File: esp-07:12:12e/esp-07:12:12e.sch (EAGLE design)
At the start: 5 parts, among them J1 ESP-STACK-HEADER

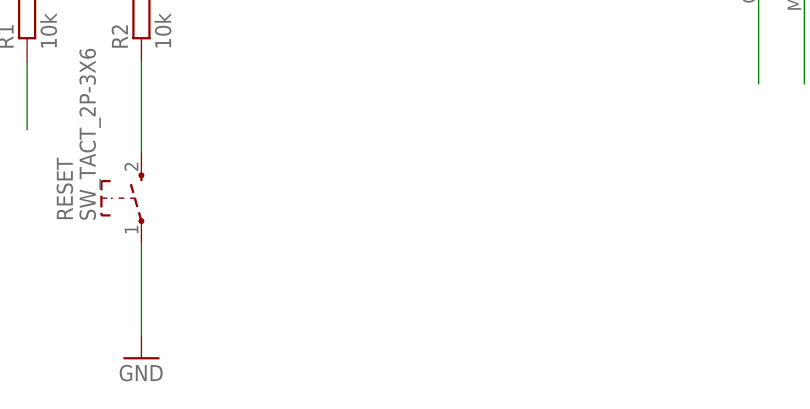
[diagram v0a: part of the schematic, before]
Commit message: Added capacitor for power stability
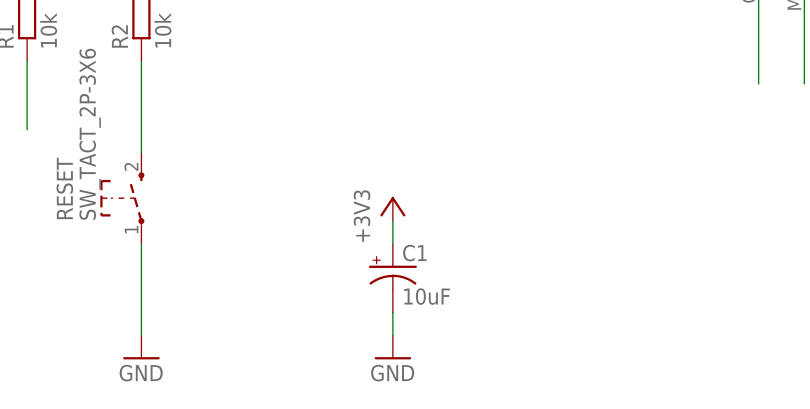
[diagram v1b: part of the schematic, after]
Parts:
- added C1: 10uF, SparkFun-Capacitors:10UF-16V-10%(TANT)
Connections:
- net +3V3: now also C1.+
- net GND: now also C1.-
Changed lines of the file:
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@@
 <layer number="121" name="_tsilk" color="7" fill="1" visible="yes" active="yes"/>
 <layer number="122" name="_bsilk" color="7" fill="1" visible="yes" active="yes"/>
+<layer number="125" name="_tNames" color="7" fill="1" visible="no" active="yes"/>
 <layer number="131" name="prix" color="7" fill="1" visible="yes" active="yes"/>
 <layer number="132" name="test" color="7" fill="1" visible="yes" active="yes"/>
+<layer number="144" name="Drill_legend" color="7" fill="1" visible="no" active="yes"/>
 <layer number="151" name="HeatSink" color="7" fill="1" visible="yes" active="yes"/>
 <layer number="200" name="200bmp" color="7" fill="1" visible="yes" active="yes"/>
@@
 <layer number="207" name="207bmp" color="7" fill="1" visible="yes" active="yes"/>
 <layer number="208" name="208bmp" color="7" fill="1" visible="yes" active="yes"/>
+<layer number="209" name="209bmp" color="7" fill="1" visible="no" active="yes"/>
+<layer number="210" name="210bmp" color="7" fill="1" visible="no" active="yes"/>
+<layer number="211" name="211bmp" color="7" fill="1" visible="no" active="yes"/>
+<layer number="212" name="212bmp" color="7" fill="1" visible="no" active="yes"/>
+<layer number="213" name="213bmp" color="7" fill="1" visible="no" active="yes"/>
+<layer number="214" name="214bmp" color="7" fill="1" visible="no" active="yes"/>
+<layer number="215" name="215bmp" color="7" fill="1" visible="no" active="yes"/>
+<layer number="216" name="216bmp" color="7" fill="1" visible="no" active="yes"/>
+<layer number="217" name="217bmp" color="18" fill="1" visible="no" active="no"/>
+<layer number="218" name="218bmp" color="19" fill="1" visible="no" active="no"/>
+<layer number="219" name="219bmp" color="20" fill="1" visible="no" active="no"/>
+<layer number="220" name="220bmp" color="21" fill="1" visible="no" active="no"/>
+<layer number="221" name="221bmp" color="22" fill="1" visible="no" active="no"/>
+<layer number="222" name="222bmp" color="23" fill="1" visible="no" active="no"/>
+<layer number="223" name="223bmp" color="24" fill="1" visible="no" active="no"/>
+<layer number="224" name="224bmp" color="25" fill="1" visible="no" active="no"/>
 <layer number="250" name="Descript" color="7" fill="1" visible="yes" active="yes"/>
 <layer number="251" name="SMDround" color="7" fill="1" visible="yes" active="yes"/>
@@
 <part name="U$1" library="ESP-12E" deviceset="ESP-07/12" device="_ESP-12E"/>
 <part name="P+1" library="supply1" deviceset="V+" device=""/>
+<part name="+3V5" library="supply1" deviceset="+3V3" device=""/>
+<part name="GND5" library="supply1" deviceset="GND" device=""/>
+<part name="C1" library="SparkFun-Capacitors" deviceset="10UF-16V-10%(TANT)" device="" value="10uF"/>
 </parts>
 <sheets>
@@
 <instance part="U$1" gate="G$1" x="-78.74" y="-2.54"/>
 <instance part="P+1" gate="1" x="17.78" y="43.18"/>
+<instance part="+3V5" gate="G$1" x="-104.14" y="-30.48"/>
+<instance part="GND5" gate="1" x="-104.14" y="-48.26"/>
+<instance part="C1" gate="G$1" x="-104.14" y="-38.1"/>
 </instances>
 <busses>
@@
 <wire x1="106.68" y1="-5.08" x2="106.68" y2="0" width="0.1524" layer="91"/>
 <wire x1="106.68" y1="0" x2="81.28" y2="0" width="0.1524" layer="91"/>
+</segment>
+<segment>
+<pinref part="GND5" gate="1" pin="GND"/>
+<pinref part="C1" gate="G$1" pin="-"/>
+<wire x1="-104.14" y1="-43.18" x2="-104.14" y2="-45.72" width="0.1524" layer="91"/>
 </segment>
 </net>
@@
 <wire x1="10.16" y1="35.56" x2="10.16" y2="38.1" width="0.1524" layer="91"/>
 </segment>
-</net>
+<segment>
+<pinref part="+3V5" gate="G$1" pin="+3V3"/>
+<pinref part="C1" gate="G$1" pin="+"/>
+<wire x1="-104.14" y1="-35.56" x2="-104.14" y2="-33.02" width="0.1524" layer="91"/>
+</segment>
+</net>

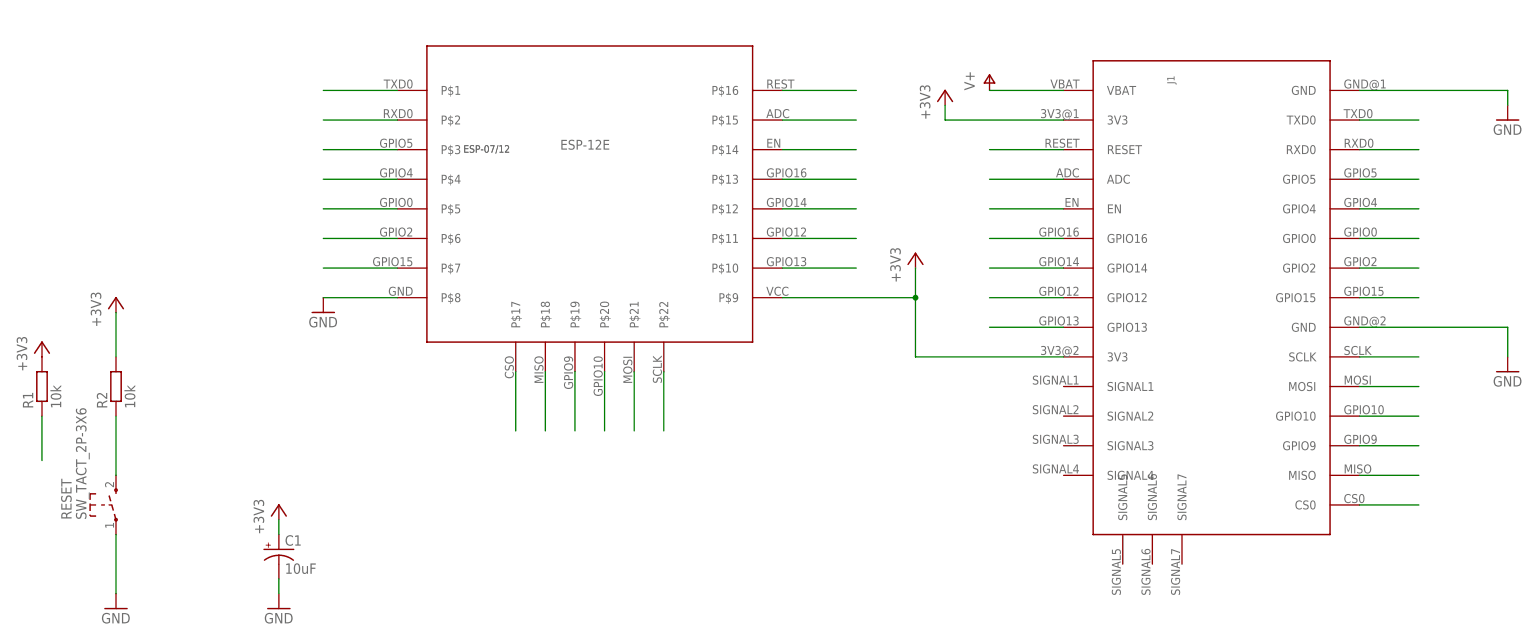
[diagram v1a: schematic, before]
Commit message: New board size - 1.4 inches; reduced number of signal pins to only two; mounting holes
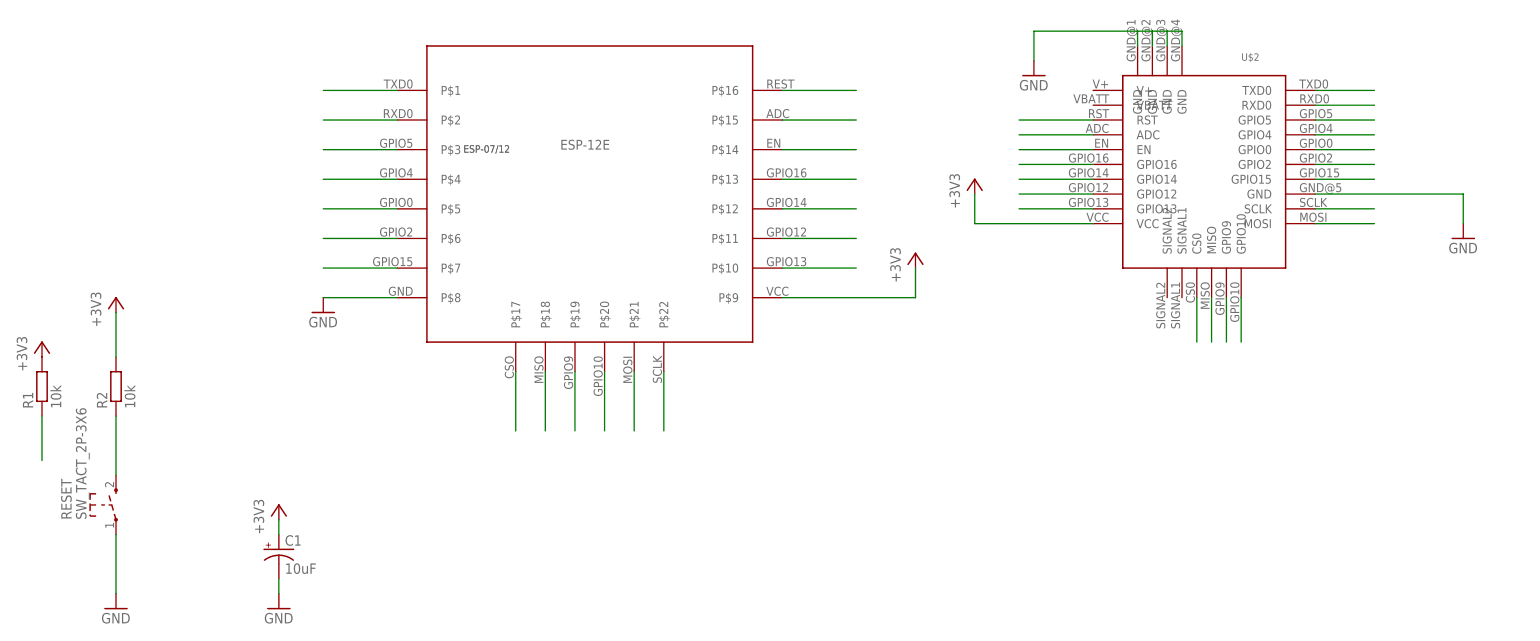
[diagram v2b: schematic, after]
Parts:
- removed J1: ESP-STACK-HEADER, ESPstack:ESP-STACK-HEADER
- added U$2: ESP-BOARD, ESPstack:ESP-BOARD
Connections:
- removed net V+: J1.VBAT
- net +3V3: now also U$2.VCC; no longer J1.3V3@1, J1.3V3@2
- net ADC: now also U$2.ADC; no longer J1.ADC
- net CS0: now also U$2.CS0; no longer J1.CS0
- net EN: now also U$2.EN; no longer J1.EN
- net GND: now also U$2.GND@1, U$2.GND@2, U$2.GND@3, U$2.GND@4, U$2.GND@5; no longer J1.GND@1, J1.GND@2
- net GPIO0: now also U$2.GPIO0; no longer J1.GPIO0
- net GPIO10: now also U$2.GPIO10; no longer J1.GPIO10
- net GPIO12: now also U$2.GPIO12; no longer J1.GPIO12
- net GPIO13: now also U$2.GPIO13; no longer J1.GPIO13
- net GPIO14: now also U$2.GPIO14; no longer J1.GPIO14
- net GPIO15: now also U$2.GPIO15; no longer J1.GPIO15
- net GPIO16: now also U$2.GPIO16; no longer J1.GPIO16
- net GPIO2: now also U$2.GPIO2; no longer J1.GPIO2
- net GPIO4: now also U$2.GPIO4; no longer J1.GPIO4
- net GPIO5: now also U$2.GPIO5; no longer J1.GPIO5
- net GPIO9: now also U$2.GPIO9; no longer J1.GPIO9
- net MISO: now also U$2.MISO; no longer J1.MISO
- net MOSI: now also U$2.MOSI; no longer J1.MOSI
- net RESET: now also U$2.RST; no longer J1.RESET
- net RXD0: now also U$2.RXD0; no longer J1.RXD0
- net SCLK: now also U$2.SCLK; no longer J1.SCLK
- net TXD0: now also U$2.TXD0; no longer J1.TXD0
